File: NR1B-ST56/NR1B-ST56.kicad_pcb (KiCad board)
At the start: 2 copper layers, 70.5 x 134 mm, 13 parts, among them J1 Conn_02x04_Odd_Even, J2 Conn_02x04_Odd_Even, J3 Conn_01x02, U1 S29GL01GP, U2 DG419LDY, X1 NUCLEO144-ZIO

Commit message: NR1B-ST56 1.0 RC 1
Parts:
- added C4: 0.1uF, Capacitor_SMD:C_0805_2012Metric, F.Cu at (199.2, 120.0)
- added C5: 47uF 16V, Capacitor_SMD:CP_Elec_5x5.3, F.Cu at (179.5, 116.2)
- added D1: S1G, Diode_SMD:D_SOD-323, F.Cu at (180.0, 98.0)
- added D2: 15V, Diode_SMD:D_SOD-323, F.Cu at (180.0, 95.5)
- added D3: S1G, Diode_SMD:D_SOD-323, F.Cu at (175.5, 123.0)
- added D4: 5.1V, Diode_SMD:D_SOD-323, F.Cu at (183.5, 123.0)
- added D5: S1G, Diode_SMD:D_SOD-323, F.Cu at (205.5, 187.0)
- added D6: 15V, Diode_SMD:D_SOD-323, F.Cu at (208.0, 190.0)
- added FID1: Fiducial, Fiducial:Fiducial_0.5mm_Mask1mm, F.Cu at (166.5, 80.5)
- added FID2: Fiducial, Fiducial:Fiducial_0.5mm_Mask1mm, F.Cu at (234.0, 80.5)
- added FID3: Fiducial, Fiducial:Fiducial_0.5mm_Mask1mm, F.Cu at (234.0, 211.5)
- added R4: 1M, Resistor_SMD:R_0805_2012Metric, F.Cu at (187.5, 121.2)
- added U3: OPA189ID, Package_SO:SOIC-8_3.9x4.9mm_P1.27mm, F.Cu at (193.8, 119.8)
- J1, J2: value Conn_02x04_Odd_Even -> 0.1" Female Long Tail
- moved R2 33.7 mm to (206.9, 168.5), turned to 0 degrees
- moved C2 32.1 mm to (192.0, 168.5)
- moved U2 30.9 mm to (209.0, 119.8)
- moved C3 30.9 mm to (214.2, 120.8)
- moved R1 27.1 mm to (203.5, 168.5), turned to 0 degrees
- moved U1 20.7 mm to (205.3, 126.7)
- moved J3 15.2 mm to (203.0, 184.0)
- moved JP1 15.2 mm to (213.0, 184.0)
- moved C1 5.68 mm to (211.4, 162.5)
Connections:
- J2 pad 6: +12V -> 12V_IN
- J3 pad 1: /EVIO -> EVIO_IN
- JP1 pad 3: /EVIO -> EVIO
- U1 pad 14: ANA_VWL -> /Vwl_buf
- X1 pad 16: VCC -> VCC_IN
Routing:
- net VCC: track 0.00 -> 130.9 mm, vias 0 -> 10
- net /DQ15: track 0.00 -> 111.4 mm, vias 0 -> 3
- net /A9: track 0.00 -> 93.8 mm, vias 0 -> 2
- net /A13: track 0.00 -> 90.4 mm, vias 0 -> 1
- net /A6: track 0.00 -> 89.3 mm, vias 0 -> 2
- net /A25: track 0.00 -> 88.6 mm
- net /A14: track 0.00 -> 86.0 mm, vias 0 -> 2
- net /A10: track 0.00 -> 85.8 mm, vias 0 -> 2
- net /A2: track 0.00 -> 85.5 mm, vias 0 -> 2
- net /A8: track 0.00 -> 83.9 mm, vias 0 -> 2
- net /A5: track 0.00 -> 82.6 mm, vias 0 -> 2
- net /A21: track 0.00 -> 80.9 mm, vias 0 -> 2
- net /A18: track 0.00 -> 76.7 mm, vias 0 -> 2
- net /A7: track 0.00 -> 76.5 mm, vias 0 -> 1
- net /A22: track 0.00 -> 76.4 mm, vias 0 -> 1
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- added copper zone on F.Cu, net +12V
- added copper zone on In2.Cu, net +12V
- added copper zone on F.Cu, net GND
- added copper zone on In1.Cu, net GND
- added copper zone on In2.Cu, net GND
- added copper zone on F.Cu, net VCC
- added copper zone on In2.Cu, net VCC
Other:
- copper layers 2 -> 4
- rule pad_to_mask_clearance: 0 -> 0.0508
- board text added: "0.1270 mm / 0.1270 mm"
- board text added: "0.2540 mm"
- board text added: "1.6 mm nom."
- board text added: "4"
- board text added: "70.5000 mm x 134.0000 mm"
- board text added: "A-1"
- board text added: "A0"
- board text added: "A1"
- board text added: "A10"
- board text added: "A11"
- board text added: "A12"
- board text added: "A13"
- board text added: "A14"
- board text added: "A15"
- board text added: "A16"
- board text added: "A17"
- board text added: "A18"
- board text added: "A19"
- board text added: "A2"
- board text added: "A20"
- board text added: "A21"
- board text added: "A22"
- board text added: "A23"
- board text added: "A3"
- board text added: "A4"
- board text added: "A5"
- board text added: "A6"
- board text added: "A7"
- board text added: "A8"
- board text added: "A9"
- board text added: "BOARD CHARACTERISTICS"
- board text added: "Board Thickness:"
- board text added: "Board overall dimensions:"
- board text added: "Castellated pads:"
- board text added: "Copper Finish:"
- board text added: "Copper Layer Count:"
- board text added: "D0"
- board text added: "D1"
- board text added: "D10"
- board text added: "D11"
- board text added: "D12"
- board text added: "D13"
- board text added: "D14"
- board text added: "D15"
- board text added: "D2"
- board text added: "D3"
- board text added: "D4"
- board text added: "D5"
- board text added: "D6"
- board text added: "D7"
- board text added: "D8"
- board text added: "D9"
- board text added: "ENIG"
- board text added: "Edge card connectors:"
- board text added: "Impedance Control:"
- board text added: "Min hole diameter:"
- board text added: "Min track/spacing:"
- board text added: "NE1"
- board text added: "No"
- board text added: "Plated Board Edge:"
- board text added: "RY/~{BY}"
- board text added: "X1A"
- board text added: "X1B"

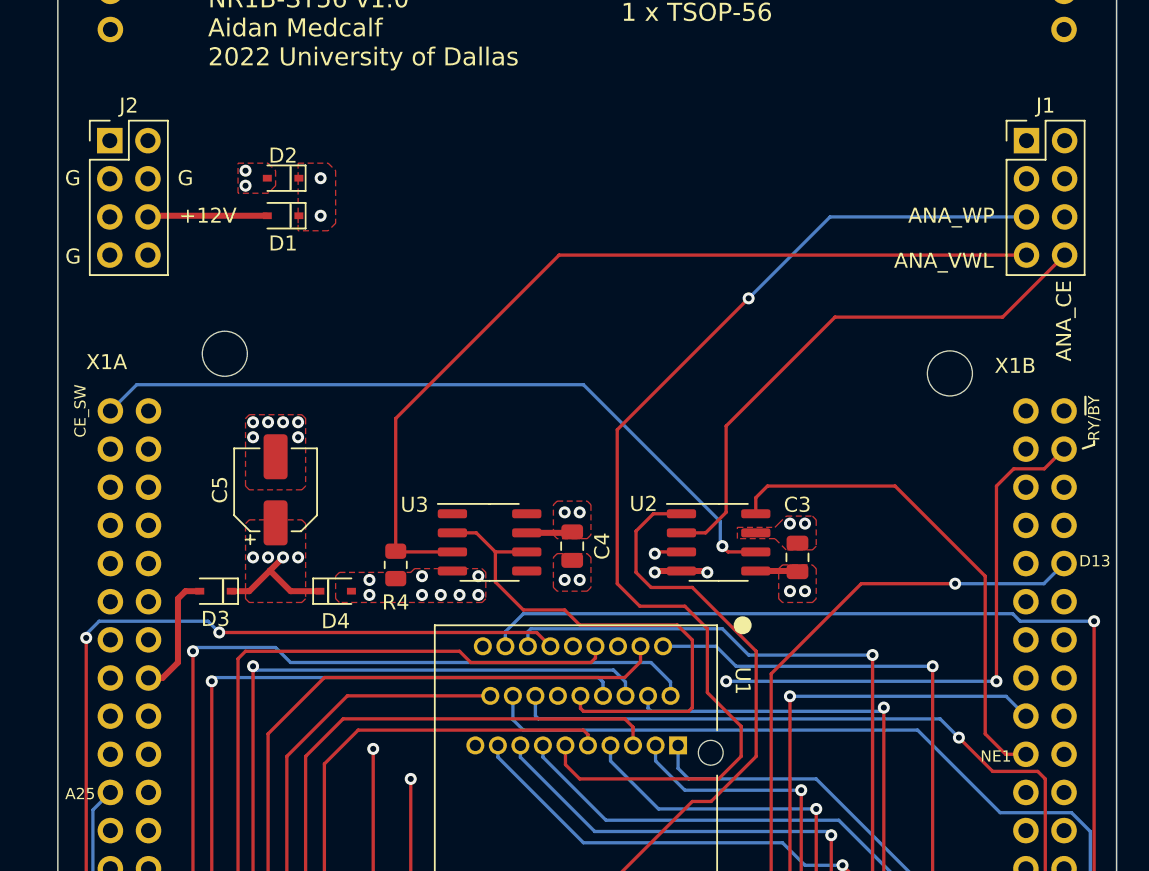
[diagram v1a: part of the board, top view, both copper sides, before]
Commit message: Added 9V for CE#; Made global labels hierarchical
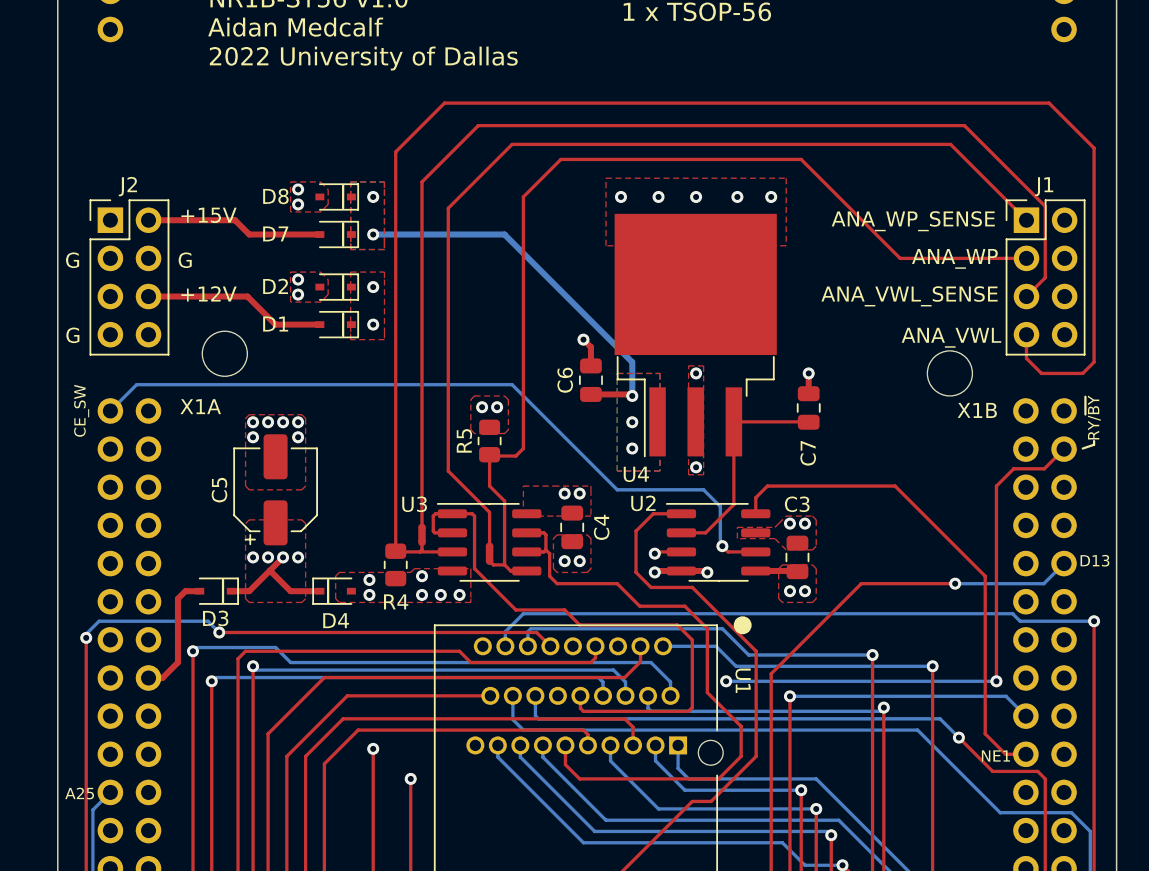
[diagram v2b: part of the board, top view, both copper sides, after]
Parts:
- added C6: 0.33uF, Capacitor_SMD:C_0805_2012Metric, F.Cu at (200.5, 109.0)
- added C7: 0.1uF, Capacitor_SMD:C_0805_2012Metric, F.Cu at (215.0, 110.8)
- added D7: S1G, Diode_SMD:D_SOD-323, F.Cu at (183.5, 99.2)
- added D8: 18V, Diode_SMD:D_SOD-323, F.Cu at (183.5, 96.8)
- added NT1: NetTie_2, NetTie:NetTie-2_SMD_Pad0.5mm, F.Cu at (189.2, 119.2)
- added NT2: NetTie_2, NetTie:NetTie-2_SMD_Pad0.5mm, F.Cu at (193.8, 120.5)
- added R5: 1M, Resistor_SMD:R_0805_2012Metric, F.Cu at (193.8, 113.0)
- added U4: NCV7800, Package_TO_SOT_SMD:TO-263-3_TabPin2, F.Cu at (207.5, 106.0)
- U3: value OPA189ID -> OPA2189ID
- moved D1 8.05 mm to (183.5, 105.2)
- moved D2 8.05 mm to (183.5, 102.8)
- moved J2 5.30 mm to (168.5, 98.3)
- moved J1 5.30 mm to (229.5, 98.3)
- moved C4 1.25 mm to (199.2, 118.8)
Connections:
- net 12V_IN renamed /12V_IN
- net ANA_VWL renamed /ANA_VWL
- net EVIO renamed /EVIO
- net EVIO_IN renamed /EVIO_IN
- net VCC_IN renamed /VCC_IN
- J1 pad 1: unconnected-(J1-Pad1) -> /ANA_WP_SENSE
- J1 pad 3: unconnected-(J1-Pad3) -> /ANA_WP
- J1 pad 5: ANA_WP -> /ANA_VWL_SENSE
- J1 pad 8: ANA_CE -> unconnected-(J1-Pad8)
- J2 pad 2: unconnected-(J2-Pad2) -> /+15V_IN
- U1 pad 14: /Vwl_buf -> /VWL_BUF
- U1 pad 16: ANA_WP -> /WP_BUF
- U2 pad 2: ANA_CE -> /ANA_CE
- U3 pad 1: (no net) -> /VWL_BUF
- U3 pad 2: /Vwl_buf -> /VWL_BUF
- U3 pad 5: (no net) -> /ANA_WP
- U3 pad 6: /Vwl_buf -> /WP_BUF
- U3 pad 7: +12V -> /WP_BUF
- U3 pad 8: (no net) -> +12V
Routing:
- net /ANA_VWL_SENSE: track 0.00 -> 74.8 mm
- net ANA_WP: track 74.0 -> 0.00 mm, vias 1 -> 0
- net /ANA_WP: track 0.00 -> 67.0 mm
- net /ANA_WP_SENSE: track 0.00 -> 66.0 mm
- net /ANA_VWL: track 59.1 -> 101.2 mm
- net /WP_BUF: track 0.00 -> 40.9 mm
- net /VWL_BUF: track 0.00 -> 38.1 mm
- net ANA_CE: track 36.5 -> 0.00 mm
- net /Vwl_buf: track 35.2 -> 0.00 mm
- net +15V: track 0.00 -> 25.8 mm, vias 0 -> 5
- net /ANA_CE: track 0.00 -> 14.8 mm
- net /+15V_IN: track 0.00 -> 11.8 mm
- net +12V: track 35.3 -> 24.5 mm
- net /12V_IN: track 7.98 -> 12.2 mm
- net GND: track 3.00 -> 6.30 mm, vias 28 -> 39
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- added copper zone on B.Cu, net +15V
- added copper zone on F.Cu, net +15V
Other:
- board text added: "+15V"
- board text added: "0.2200 mm / 0.1270 mm"
- board text added: "ANA_VWL_SENSE"
- board text added: "ANA_WP_SENSE"
- board text removed: "0.1270 mm / 0.1270 mm"
- board text removed: "ANA_CE"

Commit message: Many updates
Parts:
- removed D1: S1G, Diode_SMD:D_SOD-323
- removed D2: 15V, Diode_SMD:D_SOD-323
- added D10: 18V, Diode_SMD:D_SOD-323, F.Cu at (183.5, 104.2)
- added D9: S1G, Diode_SMD:D_SOD-323, F.Cu at (183.5, 106.8)
- added R6: 1K, Resistor_SMD:R_0805_2012Metric, F.Cu at (199.4, 119.2)
- added R7: 1K, Resistor_SMD:R_0805_2012Metric, F.Cu at (199.4, 122.8)
- U3: footprint Package_SO:SOIC-8_3.9x4.9mm_P1.27mm -> Package_SO:VSSOP-8_3.0x3.0mm_P0.65mm
- moved C4 5.14 mm to (194.8, 121.4), turned to 180 degrees
- moved U3 1.81 mm to (194.8, 118.3)
- moved NT2 1.77 mm to (195.0, 119.2), turned to 180 degrees
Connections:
- C4 pad 1: +12V -> +15V
- C4 pad 2: GND -> -15V
- J2 pad 1: unconnected-(J2-Pad1) -> /-15V_IN
- J2 pad 6: /12V_IN -> unconnected-(J2-Pad6)
- U2 pad 4: +12V -> +15V
- U3 pad 4: GND -> -15V
- U3 pad 6: /WP_BUF -> Net-(R6-Pad1)
- U3 pad 8: +12V -> +15V
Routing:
- net +12V: track 24.5 -> 0.00 mm, vias 6 -> 0
- net /-15V_IN: track 0.00 -> 18.5 mm
- net -15V: track 0.00 -> 15.7 mm, vias 0 -> 6
- net /12V_IN: track 12.2 -> 0.00 mm
- net Net-(R6-Pad1): track 0.00 -> 5.27 mm
- net /ANA_WP: track 67.0 -> 63.3 mm
- net /VWL_BUF: track 38.1 -> 36.0 mm
- net GND: track 6.30 -> 8.32 mm, vias 39 -> 45
- net +15V: track 25.8 -> 27.6 mm, vias 5 -> 10
- net /ANA_VWL: track 101.2 -> 102.9 mm
- net /WP_BUF: track 40.9 -> 40.3 mm
- added copper zone on In2.Cu, net +15V
- added copper zone on B.Cu, net -15V
- added copper zone on F.Cu, net -15V
- added copper zone on In2.Cu, net -15V
- removed copper zone on F.Cu, net +12V
- removed copper zone on In2.Cu, net +12V
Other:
- board text added: "-15V"
- board text added: "Ext. VIO"
- board text added: "GND"
- board text added: "VCC"
- board text added: "VIO"
- board text removed: "+12V"

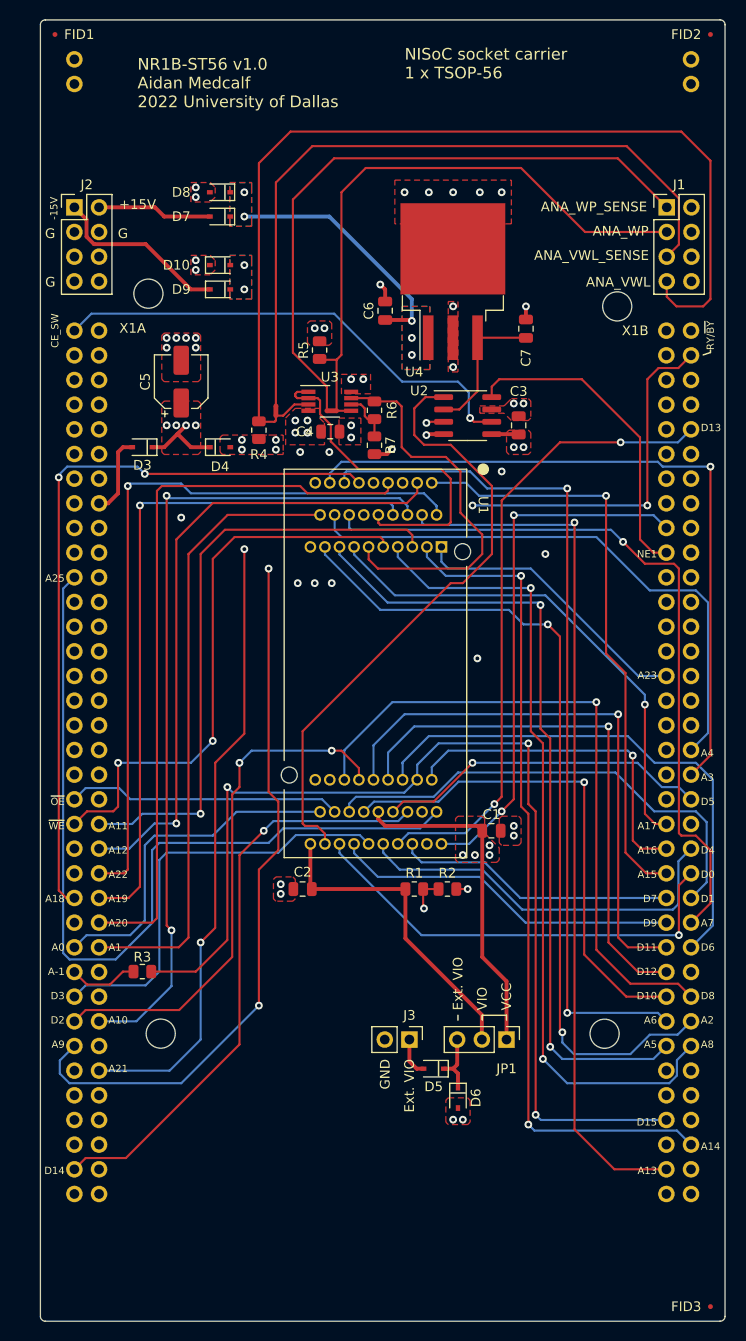
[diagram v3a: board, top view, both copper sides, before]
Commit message: Fixed footprints and silkscreen
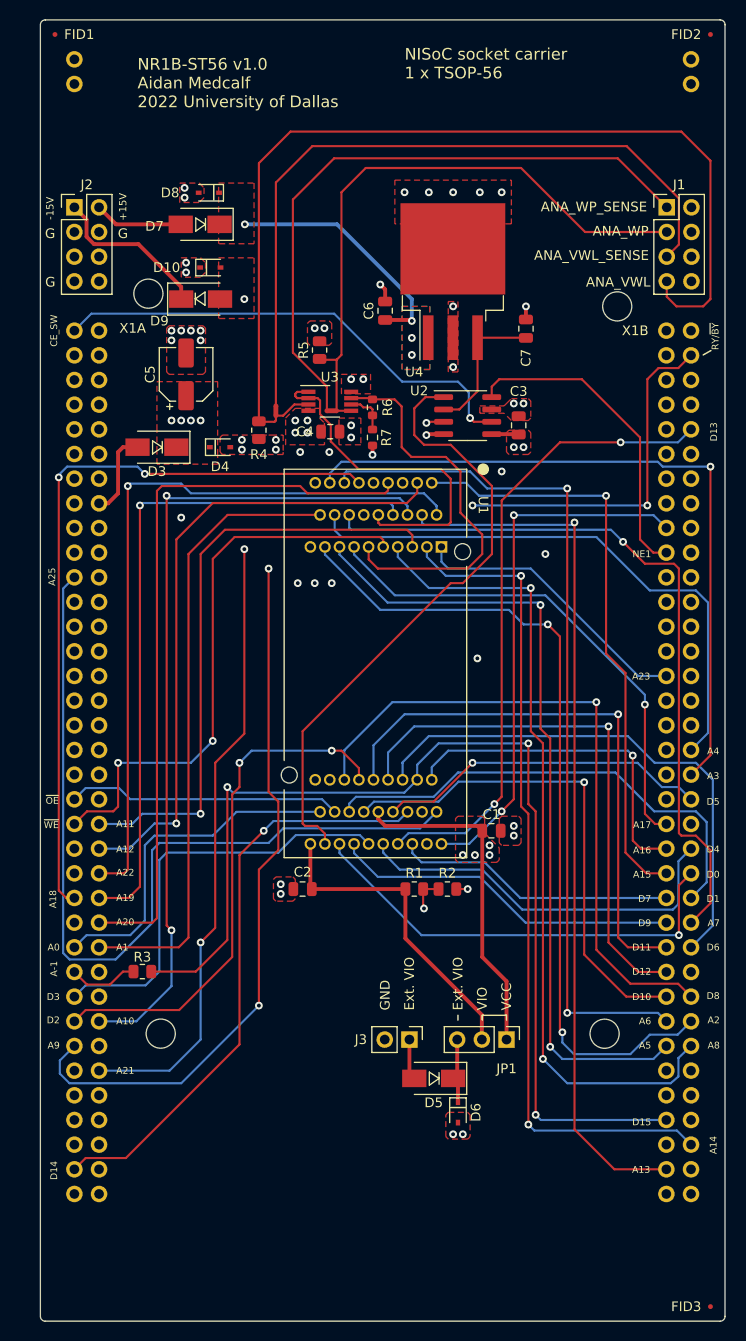
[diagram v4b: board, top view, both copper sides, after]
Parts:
- D3, D5, D7, D9: footprint Diode_SMD:D_SOD-323 -> Diode_SMD:D_SMA
- R6, R7: footprint Resistor_SMD:R_0805_2012Metric -> Resistor_SMD:R_0603_1608Metric
- moved D9 2.24 mm to (181.5, 107.8)
- moved D7 2.20 mm to (181.4, 100.0)
- moved D3 1.50 mm to (177.0, 123.0)
- moved D6 1.50 mm to (208.0, 191.5)
- moved D8 1.15 mm to (182.3, 96.8)
- moved D10 1.03 mm to (182.5, 104.5)
- moved D5 1.00 mm to (205.5, 188.0)
- moved C5 0.90 mm to (180.0, 115.5)
- moved R7 0.82 mm to (199.2, 122.0)
- moved R6 0.36 mm to (199.2, 118.9)
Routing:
- net VCC: track 130.9 -> 123.0 mm
- net /+15V_IN: track 11.8 -> 9.13 mm
- net /-15V_IN: track 18.5 -> 16.7 mm
- net GND: track 8.32 -> 7.27 mm
- net Net-(R6-Pad1): track 5.27 -> 4.48 mm
- net /VCC_IN: track 8.29 -> 8.84 mm
- net /EVIO: track 6.28 -> 6.83 mm
- net -15V: track 15.7 -> 15.3 mm, vias 6 -> 5
- net +15V: track 27.6 -> 27.2 mm, vias 10 -> 9
- removed copper zone on B.Cu, net -15V

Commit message: Added 0ohm resistors to DQ8-15 lines, updated mode instructions
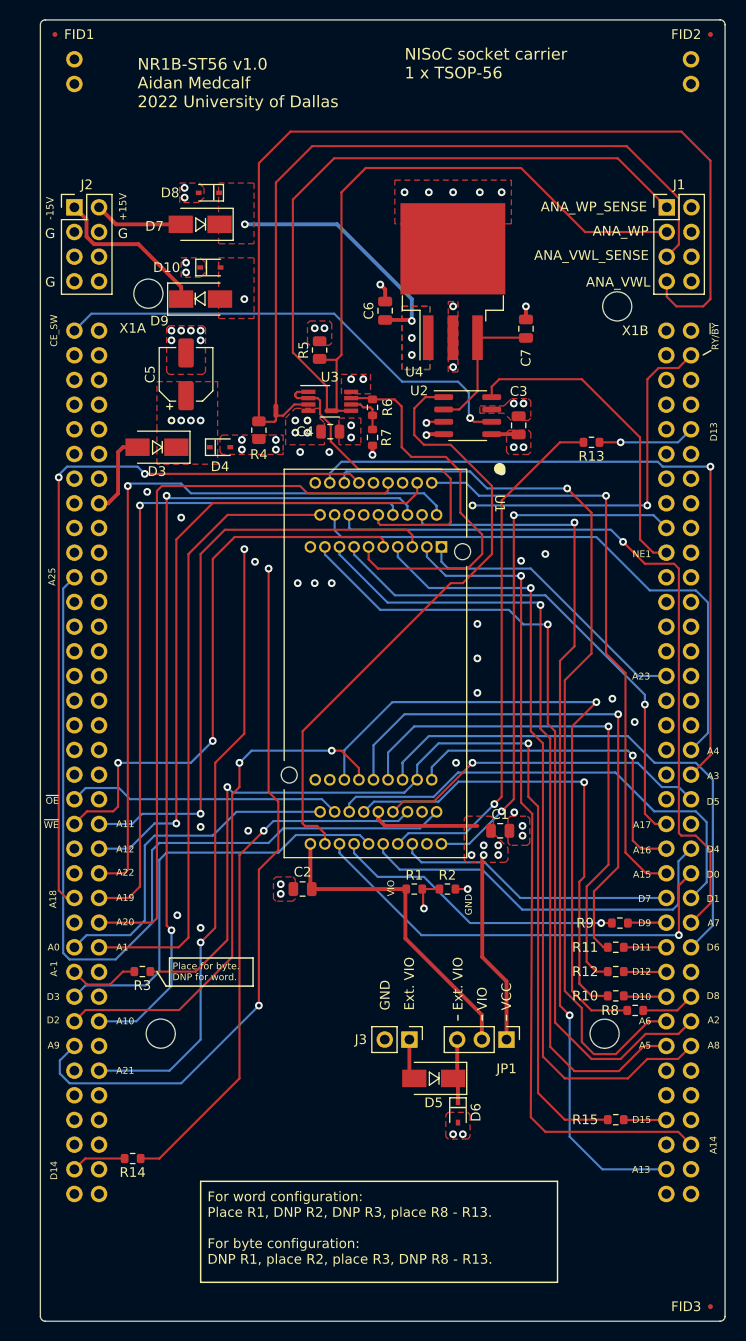
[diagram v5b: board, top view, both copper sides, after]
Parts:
- added R10: 0, Resistor_SMD:R_0603_1608Metric, F.Cu at (224.2, 179.5)
- added R11: 0, Resistor_SMD:R_0603_1608Metric, F.Cu at (224.2, 174.5)
- added R12: 0, Resistor_SMD:R_0603_1608Metric, F.Cu at (224.2, 177.0)
- added R13: 0, Resistor_SMD:R_0603_1608Metric, F.Cu at (221.8, 122.5)
- added R14: 0, Resistor_SMD:R_0603_1608Metric, F.Cu at (174.5, 196.2)
- added R15: 0, Resistor_SMD:R_0603_1608Metric, F.Cu at (224.2, 192.2)
- added R8: 0, Resistor_SMD:R_0603_1608Metric, F.Cu at (226.2, 181.0)
- added R9: 0, Resistor_SMD:R_0603_1608Metric, F.Cu at (224.7, 172.0)
- R1, R2, R3: footprint Resistor_SMD:R_0805_2012Metric -> Resistor_SMD:R_0603_1608Metric
- moved C1 0.90 mm to (212.3, 162.5)
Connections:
- X1 pad 121: /DQ9 -> Net-(R9-Pad1)
- X1 pad 123: /DQ11 -> Net-(R11-Pad1)
- X1 pad 125: /DQ12 -> Net-(R12-Pad2)
- X1 pad 127: /DQ10 -> Net-(R10-Pad2)
- X1 pad 128: /DQ8 -> Net-(R8-Pad2)
- X1 pad 137: /DQ15 -> Net-(R15-Pad1)
- X1 pad 69: /DQ14 -> Net-(R14-Pad2)
- X1 pad 82: /DQ13 -> Net-(R13-Pad1)
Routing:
- net /DQ13: track 65.7 -> 54.1 mm, vias 2 -> 1
- net VCC: track 123.0 -> 112.1 mm, vias 10 -> 11
- net Net-(R13-Pad1): track 0.00 -> 9.98 mm, vias 0 -> 1
- net /DQ15: track 111.4 -> 103.9 mm, vias 3 -> 2
- net /A6: track 89.3 -> 95.3 mm, vias 2 -> 1
- net Net-(R14-Pad2): track 0.00 -> 5.63 mm
- net /DQ9: track 36.1 -> 30.5 mm, vias 0 -> 1
- net Net-(R8-Pad2): track 0.00 -> 5.51 mm
- net /DQ14: track 61.0 -> 55.7 mm
- net Net-(R10-Pad2): track 0.00 -> 4.42 mm
- net Net-(R15-Pad1): track 0.00 -> 4.40 mm
- net Net-(R11-Pad1): track 0.00 -> 4.38 mm
- net Net-(R12-Pad2): track 0.00 -> 4.33 mm
- net Net-(R9-Pad1): track 0.00 -> 3.98 mm
- net /DQ10: track 52.0 -> 48.4 mm
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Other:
- board text added: "For word configuration: Place R1, DNP R2, DNP R3, place R8 - R13. For byte configuration: DNP R1, place R2, place R3, DNP R8 - R13."
- board text added: "Place for byte. DNP for word."
